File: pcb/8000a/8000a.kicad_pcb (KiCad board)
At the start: 2 copper layers, 53.3 x 71.1 mm, 12 parts, among them J1 Conn_01x11_Male, U1 LM339, U2 LM339, U3 MSP430G2452IPW14

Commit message: debugging the 8000A
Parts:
- removed R4: 100k, Resistor_SMD:R_0805_2012Metric
- added C1: C, Capacitor_SMD:C_0805_2012Metric, B.Cu at (77.5, 72.4)
- added C2: C, Capacitor_SMD:C_0805_2012Metric, B.Cu at (77.5, 87.6)
- added J2: USB_B, Connector_USB:USB_B_Lumberg_2411_02_Horizontal, F.Cu at (89.5, 108.6)
- added PS1: MEE3S0505SC, Converter_DCDC:Converter_DCDC_Murata_MEE3SxxxxSC_THT, F.Cu at (74.9, 108.0)
- R1: value 100k -> 150k; footprint Resistor_SMD:R_0805_2012Metric -> Resistor_THT:R_Axial_DIN0207_L6.3mm_D2.5mm_P10.16mm_Horizontal; moved to F.Cu
- R2: value 100k -> 50k; footprint Resistor_SMD:R_0805_2012Metric -> Resistor_THT:R_Axial_DIN0207_L6.3mm_D2.5mm_P10.16mm_Horizontal; moved to F.Cu
- R3: value 200k -> 100k; footprint Resistor_SMD:R_0805_2012Metric -> Resistor_THT:R_Axial_DIN0207_L6.3mm_D2.5mm_P10.16mm_Horizontal; moved to F.Cu
- moved R1 6.51 mm to (90.2, 76.2)
- moved R2 6.13 mm to (90.2, 80.0), turned to 180 degrees
- moved R3 5.08 mm to (80.0, 83.8), turned to 0 degrees
- moved U1 1.27 mm to (71.1, 72.4)
- moved U2 1.27 mm to (71.1, 87.6)
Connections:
- R2 pad 2: GND -> /VREF2
- R3 pad 1: +5V -> /VREF2
- R3 pad 2: /VREF2 -> GND
- U1 pad 1: /S1' -> /S4'
- U1 pad 10: /VREF2 -> /VREF1
- U1 pad 11: /S4 -> /S1
- U1 pad 13: /S4' -> /S1'
- U1 pad 6: /VREF1 -> /VREF2
- U1 pad 7: /S1 -> /S4
- U2 pad 1: /Z' -> /X'
- U2 pad 11: /W -> /Z
- U2 pad 13: /W' -> /Z'
- U2 pad 14: /X' -> /W'
- U2 pad 7: /Z -> /X
- U2 pad 9: /X -> /W
- U3 pad 13: unconnected-(U3-Pad13) -> /S1'
- U3 pad 9: /S1' -> /Rx
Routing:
- net GND: track 10.7 -> 89.5 mm
- net +5V: track 10.7 -> 41.8 mm
- net /S1: track 12.5 -> 37.5 mm, vias 0 -> 1
- net /~{T}: track 14.1 -> 32.8 mm, vias 0 -> 1
- net /Y: track 12.5 -> 30.5 mm, vias 0 -> 1
- net /S1': track 51.0 -> 33.5 mm
- net /Z: track 13.0 -> 29.6 mm, vias 0 -> 1
- net /S4: track 12.0 -> 26.1 mm, vias 0 -> 1
- net /S: track 12.5 -> 26.3 mm, vias 0 -> 1
- net /W: track 12.5 -> 26.3 mm, vias 0 -> 1
- net /X: track 13.0 -> 26.1 mm, vias 0 -> 1
- net /Y': track 24.8 -> 15.5 mm
- net /Z': track 24.6 -> 16.2 mm
- net /S4': track 39.3 -> 46.7 mm
- net /Rx: track 0.00 -> 6.95 mm
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
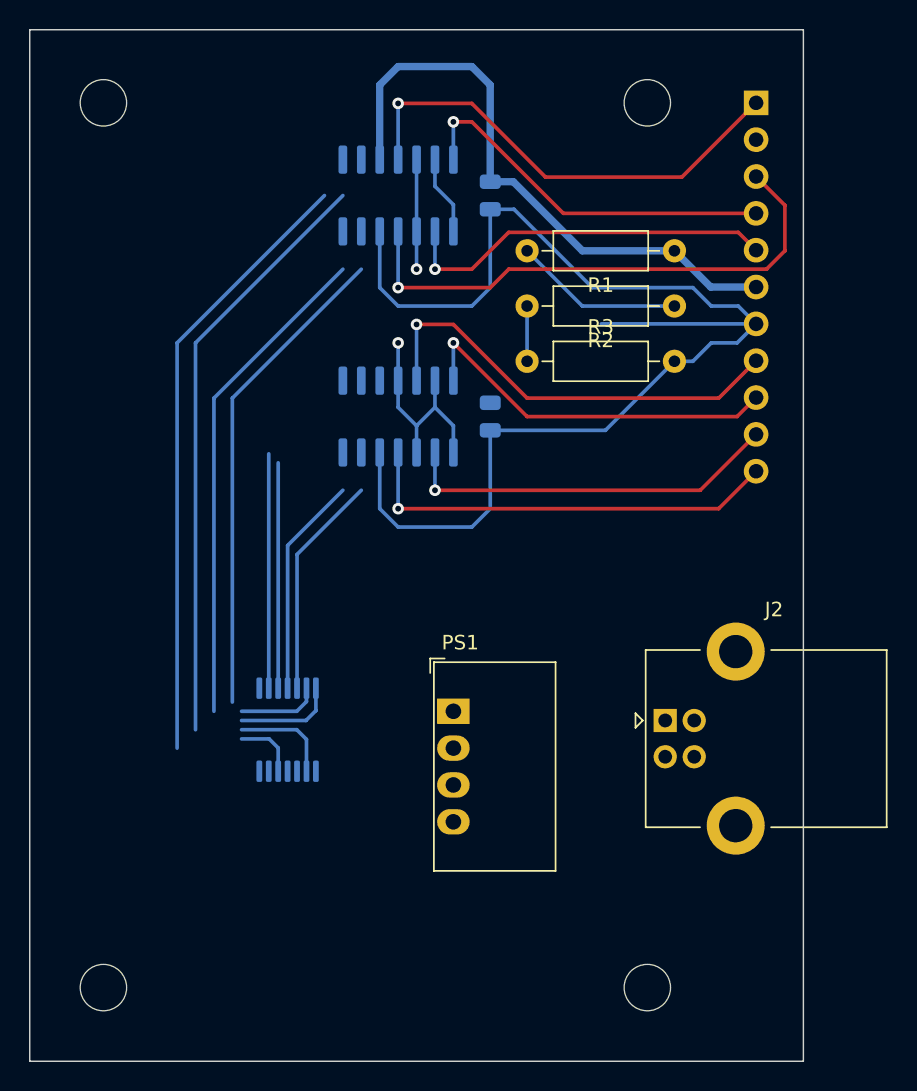
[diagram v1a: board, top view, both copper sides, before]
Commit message: put low-pass filter on S'
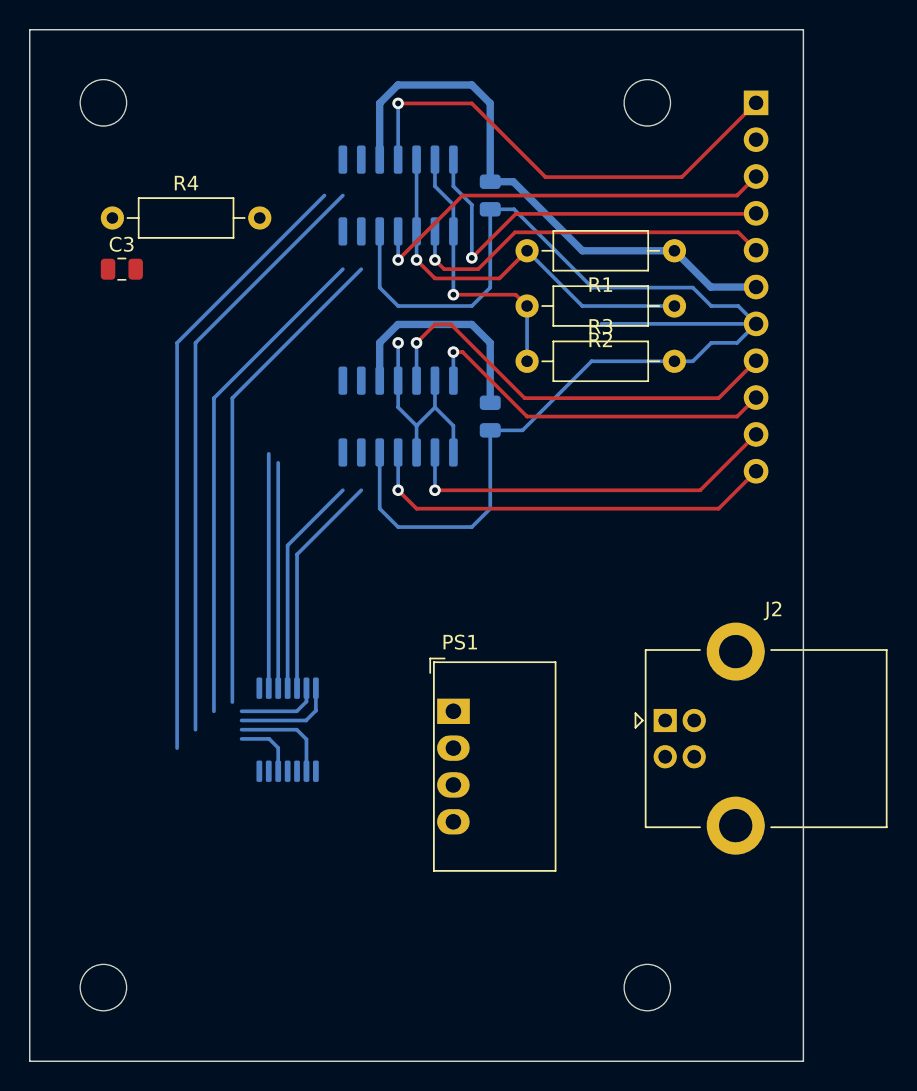
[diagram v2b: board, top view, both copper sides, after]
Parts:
- added C3: 68p, Capacitor_SMD:C_0805_2012Metric, F.Cu at (52.1, 77.5)
- added R4: 15k, Resistor_THT:R_Axial_DIN0207_L6.3mm_D2.5mm_P10.16mm_Horizontal, F.Cu at (51.4, 73.9)
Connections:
- U1 pad 14: /S' -> Net-(U1-Pad14)
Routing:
- net +5V: track 41.8 -> 54.7 mm
- net /VREF2: track 9.29 -> 19.1 mm, vias 0 -> 1
- net /S1: track 37.5 -> 29.0 mm
- net /VREF1: track 34.6 -> 42.9 mm
- net /S4: track 26.1 -> 28.2 mm
- net /X: track 26.1 -> 25.2 mm
- net /Z: track 29.6 -> 28.9 mm
- net /Y: track 30.5 -> 29.7 mm
